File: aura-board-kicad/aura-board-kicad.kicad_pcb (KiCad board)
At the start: 2 copper layers, 76.8 x 53.3 mm, 21 parts, among them J1 Power, J2 PWM_3x08, J3 BBCON, J4 Atto, J5 GPS, J6 SBUS, J7 Tele, J8 I2C0, U1 TSR2-2450, U2 PocketBeagle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

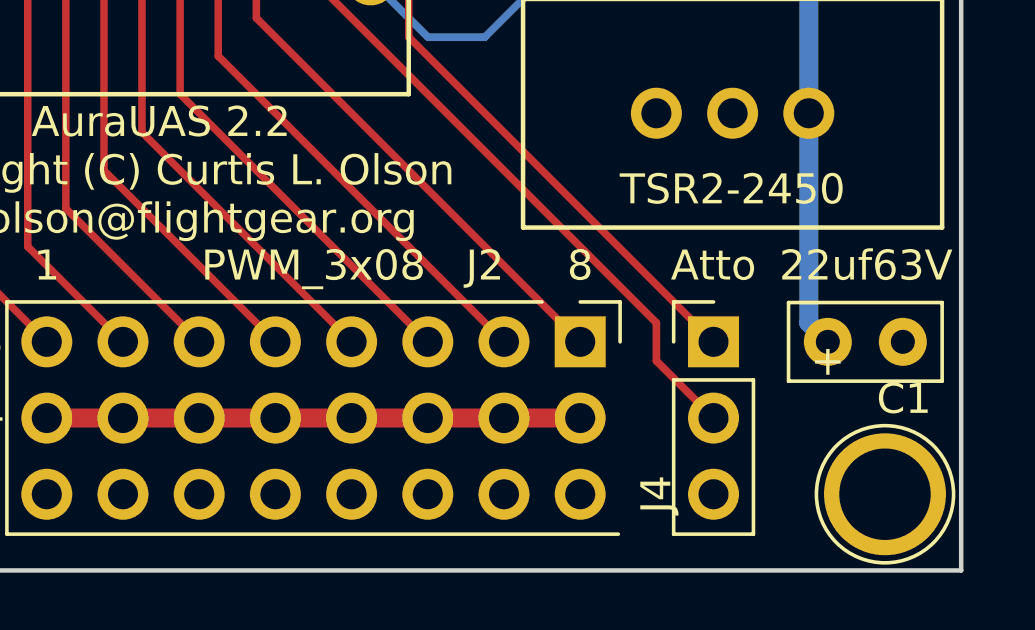
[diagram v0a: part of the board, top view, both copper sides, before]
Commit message: Label adjustments.
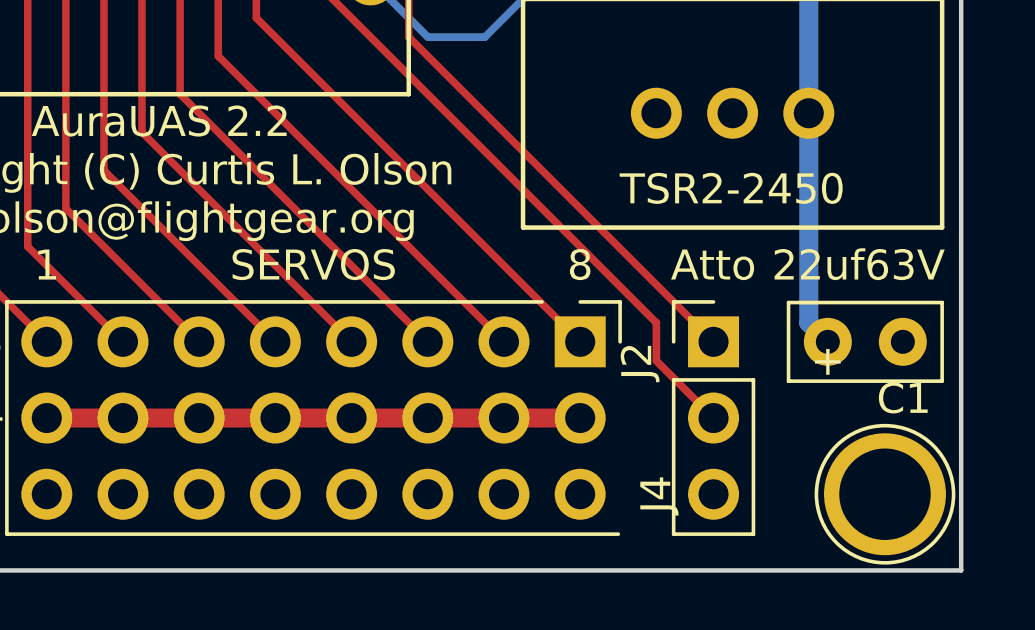
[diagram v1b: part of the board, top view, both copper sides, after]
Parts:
- J2: value PWM_3x08 -> SERVOS
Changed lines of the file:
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@@
     (descr "Through hole straight pin header, 1x08, 2.54mm pitch, single row")
     (tags "Through hole pin header THT 1x08 2.54mm single row")
-    (fp_text reference J2 (at -2.54 3.175 360) (layer F.SilkS)
-      (effects (font (size 1 1) (thickness 0.15)))
-    )
-    (fp_text value PWM_3x08 (at -2.54 8.89 360) (layer F.SilkS)
+    (fp_text reference J2 (at 0.635 -1.905 450) (layer F.SilkS)
+      (effects (font (size 1 1) (thickness 0.15)))
+    )
+    (fp_text value SERVOS (at -2.54 8.89 360) (layer F.SilkS)
       (effects (font (size 1 1) (thickness 0.15)))
     )
@@
       (effects (font (size 1 1) (thickness 0.15)))
     )
-    (fp_text value 22uf63V (at 1.27 -2.54) (layer F.SilkS)
-      (effects (font (size 1 1) (thickness 0.15)))
-    )
+    (fp_text value 22uf63V (at 1.016 -2.54) (layer F.SilkS)
+      (effects (font (size 1 1) (thickness 0.15)))
+    )

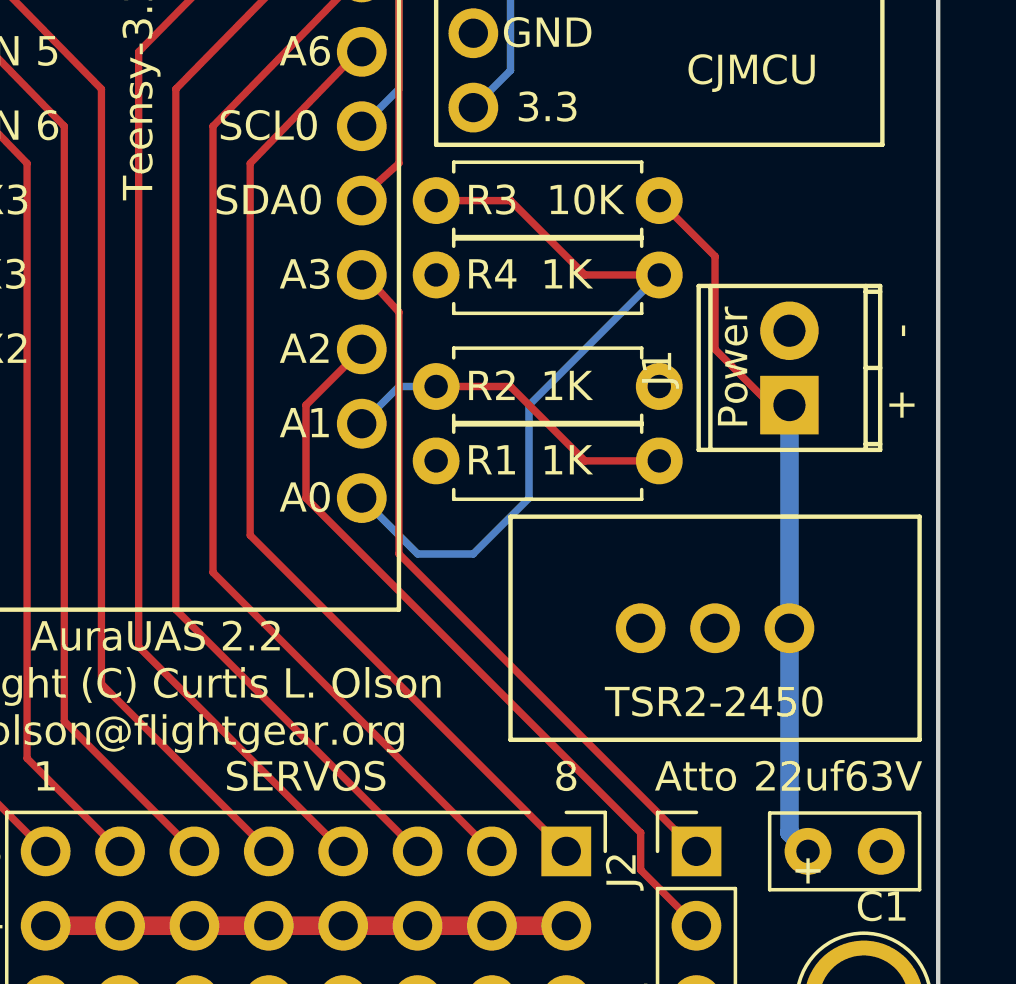
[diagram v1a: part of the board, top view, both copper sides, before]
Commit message: Switch to a larger (3.5mm) screw terminal block for main power.
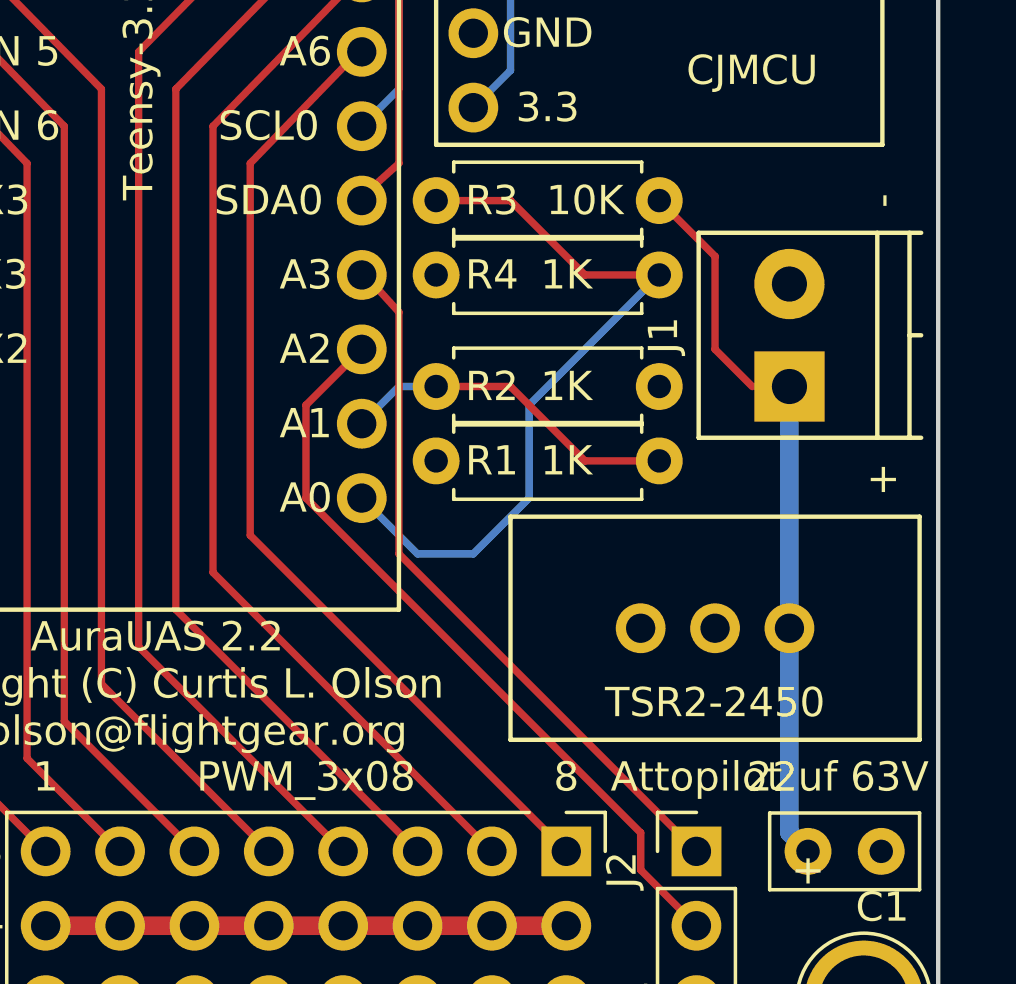
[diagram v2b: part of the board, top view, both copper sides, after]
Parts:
- C1: value 22uf63V -> 22uf 63V
- J1: value Power -> Main Power; footprint Connectors_Terminal_Blocks:TerminalBlock_Pheonix_MPT-2.54mm_2pol -> Connectors_Terminal_Blocks:TerminalBlock_Pheonix_PT-3.5mm_2pol
- J2: value SERVOS -> PWM_3x08
- J4: value Atto -> Attopilot
- moved J1 0.64 mm to (99.7, 79.4)
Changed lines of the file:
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@@
     (links 72)
     (no_connects 0)
-    (area 27.702599 48.0946 105.012401 104.3574)
+    (area 27.702599 48.0946 106.7224 104.3574)
     (thickness 1.6)
     (drawings 15)
-    (tracks 121)
+    (tracks 122)
     (zones 0)
     (modules 21)
@@
   (layers
     (0 F.Cu signal)
-    (31 B.Cu signal hide)
+    (31 B.Cu signal)
     (32 B.Adhes user)
     (33 F.Adhes user)
@@
       (effects (font (size 1 1) (thickness 0.15)))
     )
-    (fp_text value SERVOS (at -2.54 8.89 360) (layer F.SilkS)
+    (fp_text value PWM_3x08 (at -2.54 8.89 360) (layer F.SilkS)
       (effects (font (size 1 1) (thickness 0.15)))
     )
@@
       (effects (font (size 1 1) (thickness 0.15)))
     )
-    (fp_text value Atto (at 0 -2.54) (layer F.SilkS)
+    (fp_text value Attopilot (at 0 -2.54) (layer F.SilkS)
       (effects (font (size 1 1) (thickness 0.15)))
     )
@@
     )
   )
-  (module Connectors_Terminal_Blocks:TerminalBlock_Pheonix_MPT-2.54mm_2pol (layer F.Cu)
-    (at 99.695 80.01 90)
-    (descr "2-way 2.54mm pitch terminal block, Phoenix MPT series")
-    (fp_text reference J1 (at 1.27 -4.50088 90) (layer F.SilkS)
-      (effects (font (size 1 1) (thickness 0.15)))
-    )
-    (fp_text value Power (at 1.27 -1.905 90) (layer F.SilkS)
-      (effects (font (size 1 1) (thickness 0.15)))
-    )
-    (fp_line (start -1.7 -3.3) (end 4.3 -3.3) (layer F.CrtYd) (width 0.05))
-    (fp_line (start -1.7 3.3) (end -1.7 -3.3) (layer F.CrtYd) (width 0.05))
-    (fp_line (start 4.3 3.3) (end -1.7 3.3) (layer F.CrtYd) (width 0.05))
-    (fp_line (start 4.3 -3.3) (end 4.3 3.3) (layer F.CrtYd) (width 0.05))
-    (fp_line (start 4.06908 2.60096) (end -1.52908 2.60096) (layer F.SilkS) (width 0.15))
-    (fp_line (start -1.33096 3.0988) (end -1.33096 2.60096) (layer F.SilkS) (width 0.15))
-    (fp_line (start 3.87096 2.60096) (end 3.87096 3.0988) (layer F.SilkS) (width 0.15))
-    (fp_line (start 1.27 3.0988) (end 1.27 2.60096) (layer F.SilkS) (width 0.15))
-    (fp_line (start -1.52908 -2.70002) (end 4.06908 -2.70002) (layer F.SilkS) (width 0.15))
-    (fp_line (start -1.52908 3.0988) (end 4.06908 3.0988) (layer F.SilkS) (width 0.15))
-    (fp_line (start 4.06908 3.0988) (end 4.06908 -3.0988) (layer F.SilkS) (width 0.15))
-    (fp_line (start 4.06908 -3.0988) (end -1.52908 -3.0988) (layer F.SilkS) (width 0.15))
-    (fp_line (start -1.52908 -3.0988) (end -1.52908 3.0988) (layer F.SilkS) (width 0.15))
-    (pad 2 thru_hole oval (at 2.54 0 90) (size 1.99898 1.99898) (drill 1.09728) (layers *.Cu *.Mask)
-      (net 2 GND))
-    (pad 1 thru_hole rect (at 0 0 90) (size 1.99898 1.99898) (drill 1.09728) (layers *.Cu *.Mask)
-      (net 1 VDD))
-    (model Terminal_Blocks.3dshapes/TerminalBlock_Pheonix_MPT-2.54mm_2pol.wrl
-      (at (xyz 0.05 0 0))
-      (scale (xyz 1 1 1))
-      (rotate (xyz 0 0 0))
-    )
-  )
   (module Capacitors_THT:C_Disc_D5.0mm_W2.5mm_P2.50mm (layer F.Cu)
     (at 100.33 95.25)
@@
       (effects (font (size 1 1) (thickness 0.15)))
     )
-    (fp_text value 22uf63V (at 1.016 -2.54) (layer F.SilkS)
+    (fp_text value "22uf 63V" (at 1.016 -2.54) (layer F.SilkS)
       (effects (font (size 1 1) (thickness 0.15)))
     )
@@
       (net 33 "Net-(U4-Pad6)"))
   )
+  (module Connectors_Terminal_Blocks:TerminalBlock_Pheonix_PT-3.5mm_2pol (layer F.Cu)
+    (at 99.695 79.375 90)
+    (descr "2-way 3.5mm pitch terminal block, Phoenix PT series")
+    (fp_text reference J1 (at 1.75 -4.3 90) (layer F.SilkS)
+      (effects (font (size 1 1) (thickness 0.15)))
+    )
+    (fp_text value "Main Power" (at 1.75 6 90) (layer F.Fab)
+      (effects (font (size 1 1) (thickness 0.15)))
+    )
+    (fp_line (start -1.9 -3.3) (end 5.4 -3.3) (layer F.CrtYd) (width 0.05))
+    (fp_line (start -1.9 4.7) (end -1.9 -3.3) (layer F.CrtYd) (width 0.05))
+    (fp_line (start 5.4 4.7) (end -1.9 4.7) (layer F.CrtYd) (width 0.05))
+    (fp_line (start 5.4 -3.3) (end 5.4 4.7) (layer F.CrtYd) (width 0.05))
+    (fp_line (start 1.75 4.1) (end 1.75 4.5) (layer F.SilkS) (width 0.15))
+    (fp_line (start -1.75 3) (end 5.25 3) (layer F.SilkS) (width 0.15))
+    (fp_line (start -1.75 4.1) (end 5.25 4.1) (layer F.SilkS) (width 0.15))
+    (fp_line (start -1.75 -3.1) (end -1.75 4.5) (layer F.SilkS) (width 0.15))
+    (fp_line (start 5.25 4.5) (end 5.25 -3.1) (layer F.SilkS) (width 0.15))
+    (fp_line (start 5.25 -3.1) (end -1.75 -3.1) (layer F.SilkS) (width 0.15))
+    (pad 2 thru_hole circle (at 3.5 0 90) (size 2.4 2.4) (drill 1.2) (layers *.Cu *.Mask)
+      (net 2 GND))
+    (pad 1 thru_hole rect (at 0 0 90) (size 2.4 2.4) (drill 1.2) (layers *.Cu *.Mask)
+      (net 1 VDD))
+    (model Terminal_Blocks.3dshapes/TerminalBlock_Pheonix_PT-3.5mm_2pol.wrl
+      (at (xyz 0 0 0))
+      (scale (xyz 1 1 1))
+      (rotate (xyz 0 0 0))
+    )
+  )
   (gr_text "AuraUAS 2.2\nCopyright (C) Curtis L. Olson\ncurtolson@flightgear.org" (at 78.105 89.535) (layer F.SilkS)
     (effects (font (size 1 1) (thickness 0.15)))
@@
     (effects (font (size 1 1) (thickness 0.25)))
   )
-  (gr_text - (at 103.505 77.47 90) (layer F.SilkS)
+  (gr_text - (at 102.87 73.025 90) (layer F.SilkS)
     (effects (font (size 1 1) (thickness 0.25)))
   )
-  (gr_text + (at 103.505 80.01 90) (layer F.SilkS)
+  (gr_text + (at 102.87 82.55 90) (layer F.SilkS)
     (effects (font (size 1 1) (thickness 0.25)))
   )
@@
   (gr_line (start 29.21 102.87) (end 104.775 102.87) (angle 90) (layer Edge.Cuts) (width 0.15))
   (gr_line (start 27.94 49.53) (end 27.94 102.87) (angle 90) (layer Edge.Cuts) (width 0.15))
+  (segment (start 95.25 73.025) (end 97.155 74.93) (width 0.254) (layer F.Cu) (net 1) (status 400000))
+  (segment (start 98.425 79.375) (end 99.695 79.375) (width 0.1524) (layer F.Cu) (net 1) (status 800000))
+  (segment (start 97.155 78.105) (end 98.425 79.375) (width 0.254) (layer F.Cu) (net 1))
+  (segment (start 97.155 74.93) (end 97.155 78.105) (width 0.254) (layer F.Cu) (net 1))
   (segment (start 99.695 80.01) (end 99.06 80.01) (width 0.635) (layer F.Cu) (net 1))
-  (segment (start 99.06 80.01) (end 97.155 78.105) (width 0.254) (layer F.Cu) (net 1))
-  (segment (start 97.155 74.93) (end 95.25 73.025) (width 0.254) (layer F.Cu) (net 1))
-  (segment (start 97.155 78.105) (end 97.155 74.93) (width 0.254) (layer F.Cu) (net 1))
   (segment (start 99.695 87.63) (end 99.695 80.01) (width 0.635) (layer B.Cu) (net 1))
   (segment (start 100.33 95.25) (end 99.695 94.615) (width 0.635) (layer B.Cu) (net 1))
